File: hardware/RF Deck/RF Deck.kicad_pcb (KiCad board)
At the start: 2 copper layers, 76.2 x 127 mm, 57 parts, among them J1 RadioBNC, J10 AntennaSMA, J11 Dummy Load, J12 To Digital Deck, J13 Ant/Dummy, J14 Tx/Rx, J2 RadioSMA, J3 High Impedance Tap, J4 Low Impedance Tap, J5 Frequency Counter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

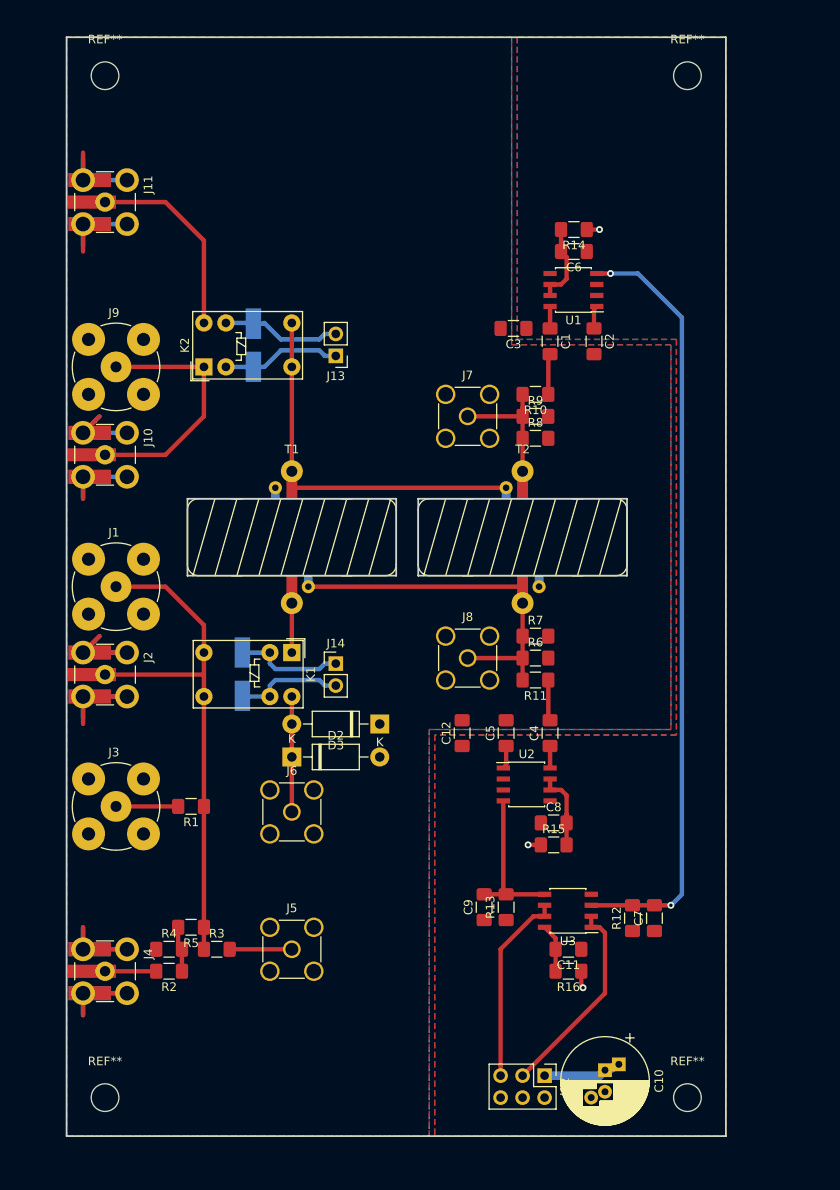
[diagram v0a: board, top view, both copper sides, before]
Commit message: Updated silkscreen and moved a few things around. AS ORDERED 2019-11-02
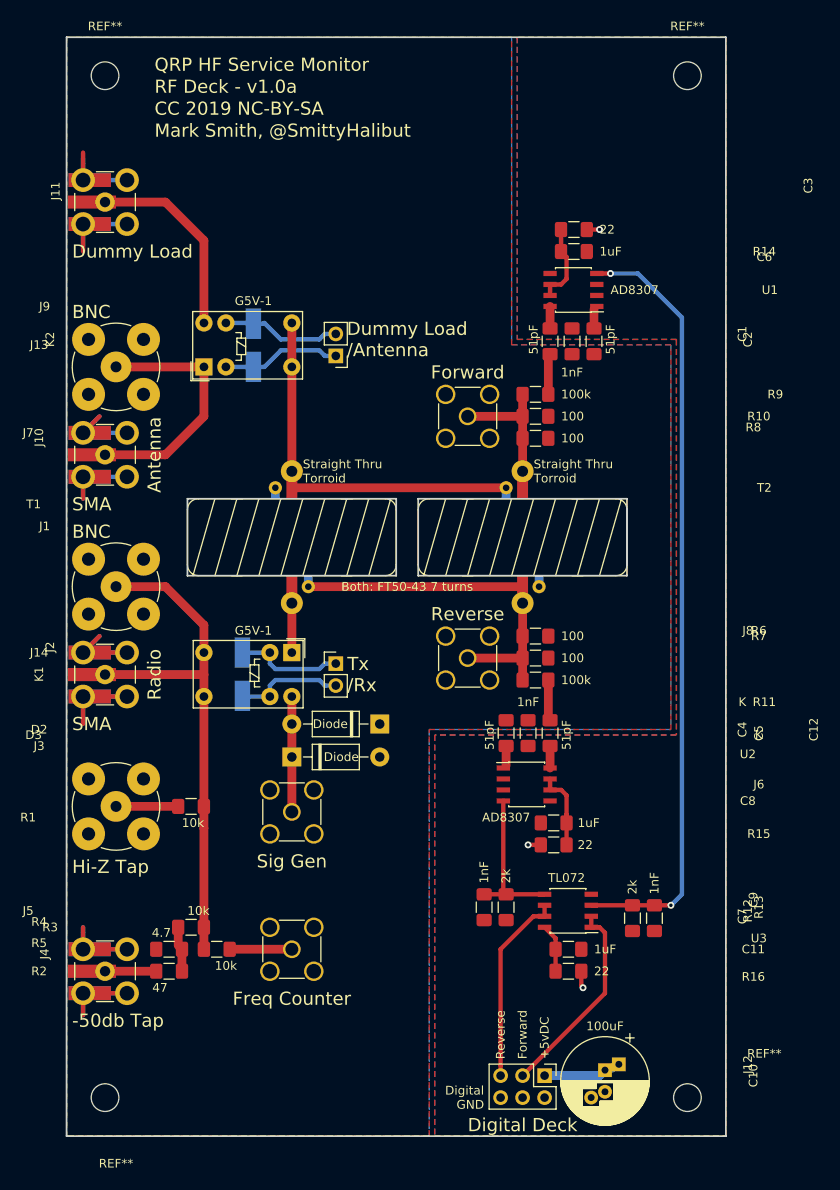
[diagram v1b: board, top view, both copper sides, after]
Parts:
- moved C12 7.62 mm to (97.8, 105.8)
- moved C3 6.93 mm to (102.9, 60.5), turned to 270 degrees
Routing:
- net Net-(K1-Pad1): track 5.71 -> 7.62 mm
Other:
- board text added: "+5vDC"
- board text added: "-50db Tap"
- board text added: "100"
- board text added: "100k"
- board text added: "100uF"
- board text added: "10k"
- board text added: "1nF"
- board text added: "1uF"
- board text added: "22"
- board text added: "2k"
- board text added: "4.7"
- board text added: "47"
- board text added: "51pF"
- board text added: "<><"
- board text added: "><>"
- board text added: "AD8307"
- board text added: "Antenna"
- board text added: "BNC"
- board text added: "Both: FT50-43 7 turns"
- board text added: "CC 2019 NC-BY-SA"
- board text added: "Digital Deck"
- board text added: "Digital GND"
- board text added: "Diode"
- board text added: "Dummy Load"
- board text added: "Dummy Load /Antenna"
- board text added: "Forward"
- board text added: "Freq Counter"
- board text added: "G5V-1"
- board text added: "Hi-Z Tap"
- board text added: "Mark Smith, @SmittyHalibut"
- board text added: "O"
- board text added: "QRP HF Service Monitor"
- board text added: "RF Deck - v1.0a"
- board text added: "Radio"
- board text added: "Reverse"
- board text added: "SMA"
- board text added: "Sig Gen"
- board text added: "Straight Thru Torroid"
- board text added: "TL072"
- board text added: "Tx /Rx"
- board text added: "o"
